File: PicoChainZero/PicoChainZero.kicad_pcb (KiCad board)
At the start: 4 copper layers, 60 x 34 mm, 19 parts, among them J1 RJ45, J2 RJ45, J3 +12V, J4 +5V(M), J5 I2C, J6 +5V, U1 LM78M05, U2 LM78M05, U3 LM1085, U4 PCA9615DP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

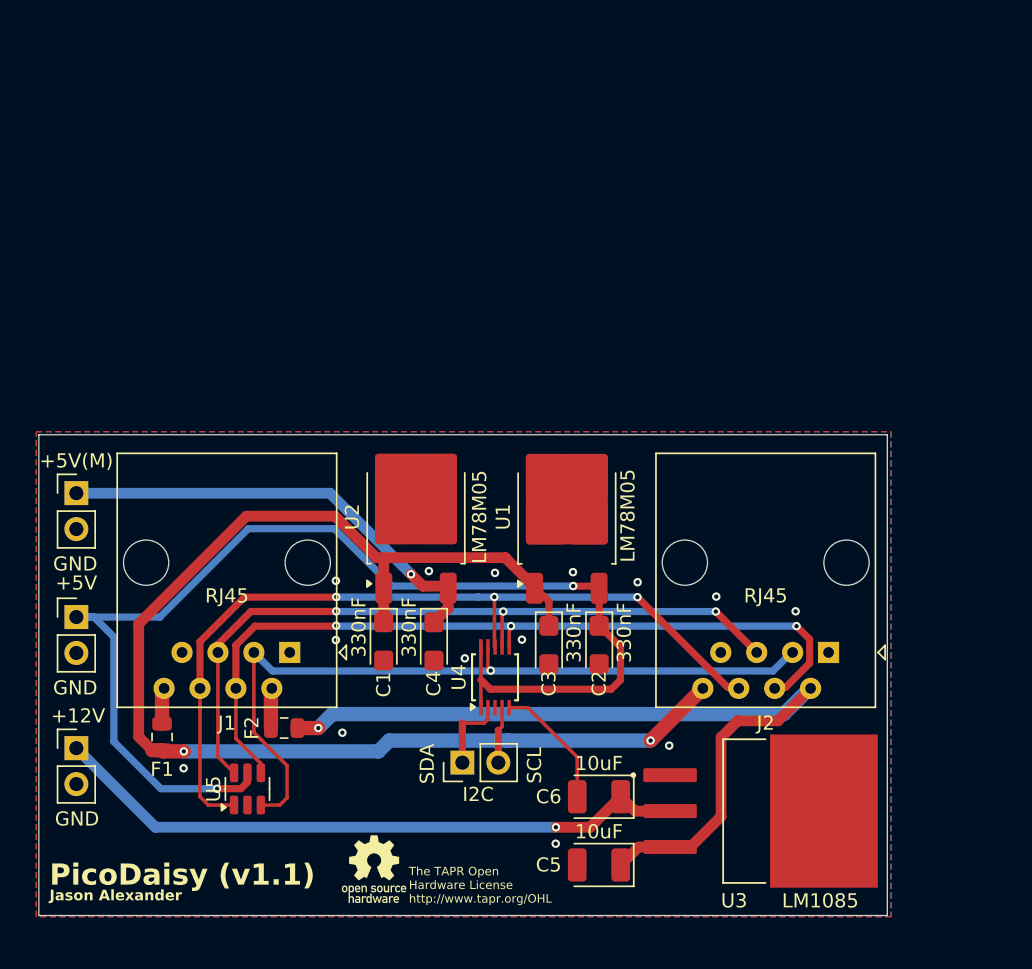
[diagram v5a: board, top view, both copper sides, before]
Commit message: Updated PicoChainZero PCB layout and generated Gerbers.
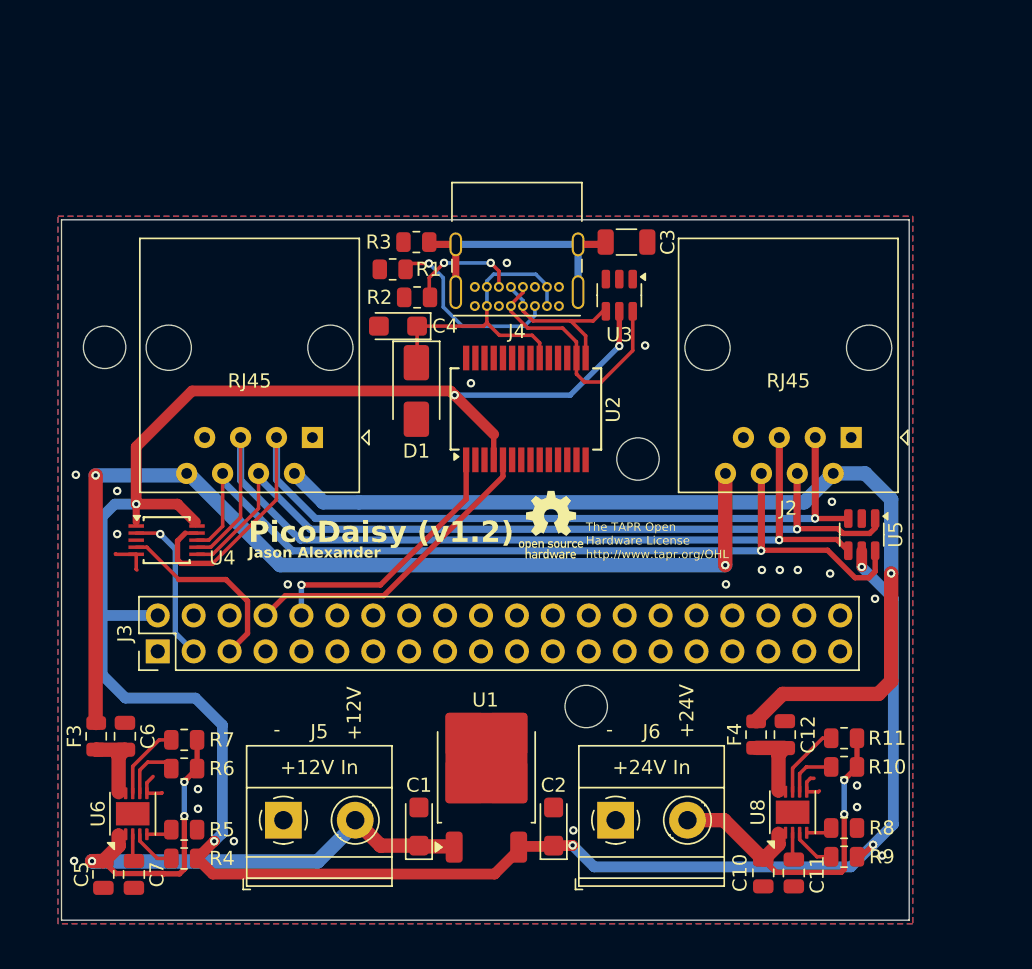
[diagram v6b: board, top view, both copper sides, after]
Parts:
- removed F1, F2: Fuse, Fuse:Fuse_0805_2012Metric
- added C10: 10uF, Capacitor_SMD:C_0805_2012Metric, F.Cu at (151.2, 97.0)
- added C11: 47nF, Capacitor_SMD:C_0805_2012Metric, F.Cu at (153.4, 97.0)
- added C12: 10uF, Capacitor_SMD:C_0805_2012Metric, F.Cu at (152.8, 87.2)
- added C7: 47nF, Capacitor_SMD:C_0805_2012Metric, F.Cu at (106.7, 97.1)
- added D1: D_Schottky, Diode_SMD:D_SMA, F.Cu at (126.7, 62.9)
- added F3: Fuse, Fuse:Fuse_0805_2012Metric, F.Cu at (104.1, 87.3)
- added F4: Fuse, Fuse:Fuse_0805_2012Metric, F.Cu at (150.7, 87.2)
- added R1: 5.1K, Resistor_SMD:R_0805_2012Metric, F.Cu at (125.0, 54.3)
- added R10: 100K, Resistor_SMD:R_0805_2012Metric, F.Cu at (156.9, 89.5)
- added R11: 100K, Resistor_SMD:R_0805_2012Metric, F.Cu at (156.9, 87.5)
- added R2: 5.1K, Resistor_SMD:R_0805_2012Metric, F.Cu at (126.7, 56.3)
- added R3: 470K, Resistor_SMD:R_0805_2012Metric, F.Cu at (126.7, 52.4)
- added R4: 470K, Resistor_SMD:R_0805_2012Metric, F.Cu at (110.3, 96.0)
- added R5: 2K, Resistor_SMD:R_0805_2012Metric, F.Cu at (110.3, 93.9)
- added R6: 100K, Resistor_SMD:R_0805_2012Metric, F.Cu at (110.3, 89.6)
- added R7: 100K, Resistor_SMD:R_0805_2012Metric, F.Cu at (110.3, 87.6)
- added R8: 2K, Resistor_SMD:R_0805_2012Metric, F.Cu at (156.9, 93.8)
- added R9: 470K, Resistor_SMD:R_0805_2012Metric, F.Cu at (156.9, 95.8)
- added U6: SiP32419, Package_DFN_QFN:DFN-10-1EP_3x3mm_P0.5mm_EP1.65x2.38mm, F.Cu at (106.6, 92.8)
- added U8: SiP32419, Package_DFN_QFN:DFN-10-1EP_3x3mm_P0.5mm_EP1.65x2.38mm, F.Cu at (153.3, 92.7)
- C3: value 330nF -> 1nF; footprint Capacitor_Tantalum_SMD:CP_EIA-3216-18_Kemet-A -> Capacitor_SMD:C_1206_3216Metric
- C4: value 330nF -> 10uF
- C5, C6: footprint Capacitor_Tantalum_SMD:CP_EIA-3528-21_Kemet-B -> Capacitor_SMD:C_0805_2012Metric
- J3: value +12V -> Raspberry Pi; footprint Connector_PinHeader_2.54mm:PinHeader_1x02_P2.54mm_Vertical -> Connector_PinHeader_2.54mm:PinHeader_2x20_P2.54mm_Vertical
- J4: value +5V(M) -> USB_C_Receptacle_USB2.0_14P; footprint Connector_PinHeader_2.54mm:PinHeader_1x02_P2.54mm_Vertical -> Connector_USB:USB_C_Receptacle_GCT_USB4085
- J5: value I2C -> +12V In; footprint Connector_PinHeader_2.54mm:PinHeader_1x02_P2.54mm_Vertical -> TerminalBlock_Phoenix:TerminalBlock_Phoenix_MKDS-1,5-2-5.08_1x02_P5.08mm_Horizontal
- J6: value +5V -> +24V In; footprint Connector_PinHeader_2.54mm:PinHeader_1x02_P2.54mm_Vertical -> TerminalBlock_Phoenix:TerminalBlock_Phoenix_MKDS-1,5-2-5.08_1x02_P5.08mm_Horizontal
- U2: value LM78M05 -> FT232RL; footprint Package_TO_SOT_SMD:TO-252-2 -> Package_SO:SSOP-28_5.3x10.2mm_P0.65mm
- U3: value LM1085 -> SRV05; footprint LM1085IS-12:TO254P1524X483-4N -> Package_TO_SOT_SMD:SOT-23-6
- moved U5 47.0 mm to (158.2, 73.1), turned to -90 degrees
- moved J6 40.8 mm to (140.8, 93.3)
- moved U3 37.8 mm to (141.0, 56.1), turned to -90 degrees
- moved J4 36.6 mm to (136.8, 56.9), turned to 180 degrees
- moved C5 35.1 mm to (104.6, 97.1), turned to 90 degrees
- moved C6 33.8 mm to (106.1, 87.3), turned to -90 degrees
- moved C3 29.0 mm to (141.6, 52.4), turned to 0 degrees
- moved U4 25.2 mm to (109.0, 73.5), turned to 0 degrees
- moved C4 22.4 mm to (125.4, 58.3), turned to 180 degrees
- moved U1 19.2 mm to (131.6, 90.1)
- moved J1 15.3 mm to (119.3, 66.2)
- moved J2 15.3 mm to (157.4, 66.2)
- moved C1 13.3 mm to (126.9, 93.7), turned to 90 degrees
- moved J5 13.3 mm to (117.3, 93.3), turned to 0 degrees
- moved C2 13.2 mm to (136.4, 93.7), turned to 90 degrees
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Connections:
- C1 pad 1: +12V -> Net-(J5-Pin_2)
- C3 pad 1: +12V -> Net-(J4-SHIELD)
- C4 pad 1: /+5V(M) -> Net-(D1-K)
- C5 pad 1: +24V -> GND
- C5 pad 2: GND -> Net-(J5-Pin_2)
- C6 pad 1: /+12V(R) -> GND
- C6 pad 2: GND -> Net-(C6-Pad2)
- J1 pad 2: Net-(F2-Pad1) -> +24V
- J1 pad 8: Net-(F1-Pad1) -> +12V
- J3 pad 1: /+12V(R) -> unconnected-(J3-Pin_1-Pad1)
- J3 pad 2: GND -> +5V
- J5 pad 1: Net-(J5-Pin_1) -> GND
- J6 pad 1: +5V -> GND
- J6 pad 2: GND -> Net-(J6-Pin_2)
- U1 pad 1: +12V -> Net-(J5-Pin_2)
- U2 pad 1: +12V -> Net-(J3-Pin_10)
- U2 pad 2: GND -> unconnected-(U2-DTR-Pad2)
- U2 pad 3: /+5V(M) -> unconnected-(U2-RTS-Pad3)
- U3 pad 1: GND -> unconnected-(U3-IO1-Pad1)
- U3 pad 2: /+12V(R) -> GND
- U3 pad 3: +24V -> unconnected-(U3-IO2-Pad3)
- U3 pad 4: (no net) -> Net-(U2-USBD+)
- U4 pad 2: Net-(J5-Pin_1) -> Net-(J3-Pin_3)
- U4 pad 4: Net-(J5-Pin_2) -> Net-(J3-Pin_5)
- U5 pad 1: Net-(U4-DSDAP) -> Net-(U4-DSCLM)
- U5 pad 4: Net-(U4-DSCLM) -> Net-(U4-DSCLP)
- U5 pad 6: Net-(U4-DSCLP) -> Net-(U4-DSDAP)
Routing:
- net +5V: track 85.7 -> 168.3 mm, vias 2 -> 7
- net /+12V(R): track 45.6 -> 0.00 mm, vias 1 -> 0
- net Net-(J5-Pin_2): track 3.99 -> 46.7 mm, vias 0 -> 3
- net /+5V(M): track 31.9 -> 0.00 mm, vias 1 -> 0
- net Net-(J6-Pin_2): track 0.00 -> 24.6 mm, vias 0 -> 2
- net Net-(J3-Pin_8): track 0.00 -> 22.0 mm
- net Net-(D1-K): track 0.00 -> 21.6 mm
- net Net-(J4-SHIELD): track 0.00 -> 19.5 mm
- net +12V: track 91.0 -> 71.5 mm
- net Net-(J3-Pin_10): track 0.00 -> 19.1 mm, vias 0 -> 1
- net Net-(U2-USBD-): track 0.00 -> 18.0 mm
- net Net-(J3-Pin_5): track 0.00 -> 13.6 mm
- net Net-(J4-CC1): track 0.00 -> 13.4 mm, vias 0 -> 1
- net Net-(U4-DSCLP): track 52.3 -> 65.0 mm, vias 3 -> 1
- net Net-(U4-DSDAM): track 54.6 -> 66.6 mm
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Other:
- board size 60 x 34 mm -> 59.9 x 49.5 mm
- board text added: "+12V"
- board text added: "+24V"
- board text added: "-"
- board text added: "PicoDaisy (v1.2)"
- board text removed: "GND"
- board text removed: "SCL"
- board text removed: "SDA"

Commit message: Updated to 1.2
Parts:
- moved J1 1.74 mm to (117.8, 65.4)
- moved J6 1.07 mm to (141.2, 94.2)
- moved J5 1.07 mm to (117.7, 94.2)
- moved R8 0.89 mm to (157.3, 93.0)
- moved D1 0.89 mm to (127.1, 62.1)
- moved R7 0.89 mm to (110.7, 86.8)
- moved C1 0.89 mm to (127.3, 92.9)
- moved C10 0.89 mm to (151.6, 96.2)
- moved C11 0.89 mm to (153.8, 96.2)
- moved C12 0.89 mm to (153.2, 86.4)
- moved C2 0.89 mm to (136.8, 92.9)
- moved C3 0.89 mm to (142.0, 51.6)
- moved C4 0.89 mm to (125.8, 57.5)
- moved C7 0.89 mm to (107.1, 96.3)
- moved F4 0.89 mm to (151.1, 86.4)
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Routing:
- net +5V: track 168.3 -> 170.6 mm
- net Net-(U4-DSDAP): track 63.1 -> 65.2 mm
- net +24V: track 68.3 -> 70.2 mm
- net Net-(U4-DSCLP): track 65.0 -> 66.7 mm
- net Net-(U4-DSDAM): track 66.6 -> 68.3 mm
- net Net-(U4-DSCLM): track 58.5 -> 60.2 mm
- net Net-(J6-Pin_2): track 24.6 -> 23.9 mm
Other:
- board size 59.9 x 49.5 mm -> 68 x 50 mm
